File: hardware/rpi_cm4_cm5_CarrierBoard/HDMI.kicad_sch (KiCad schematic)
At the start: 12 parts, among them J4 2086581001, U18 AP22913W6-7

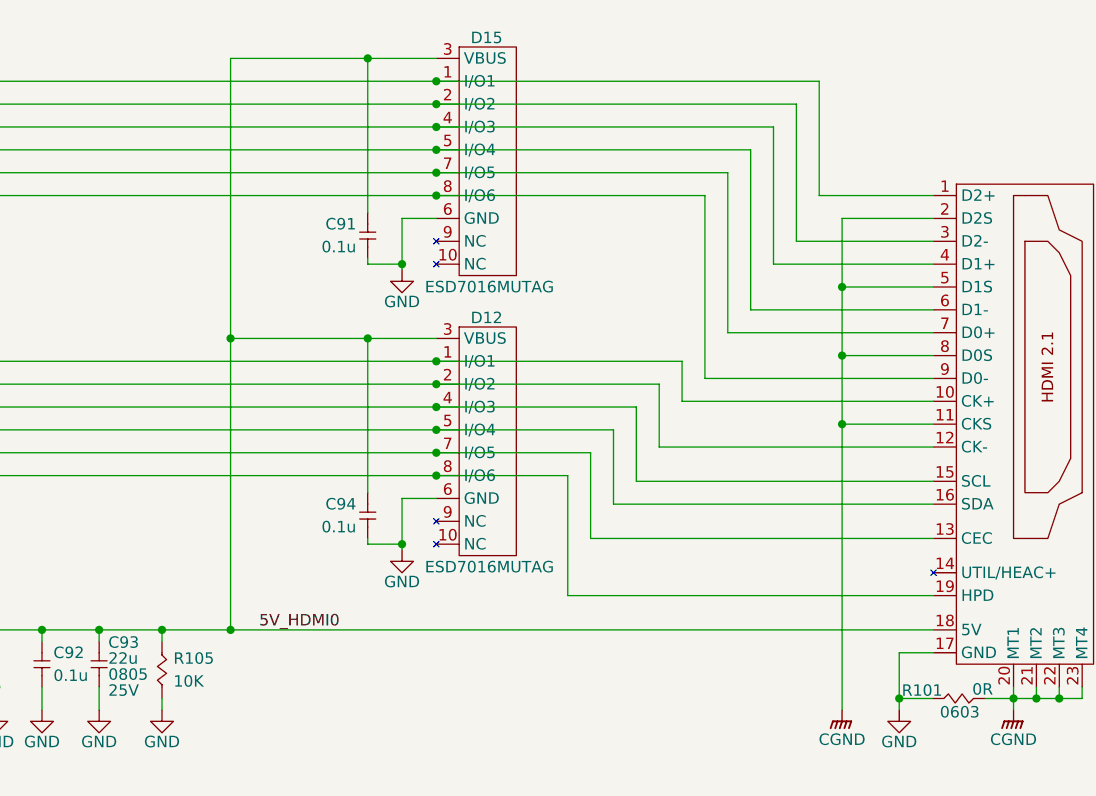
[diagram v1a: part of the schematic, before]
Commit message: Preliminary completion of RPI CMx schematics Cleaned up hierarchical root page
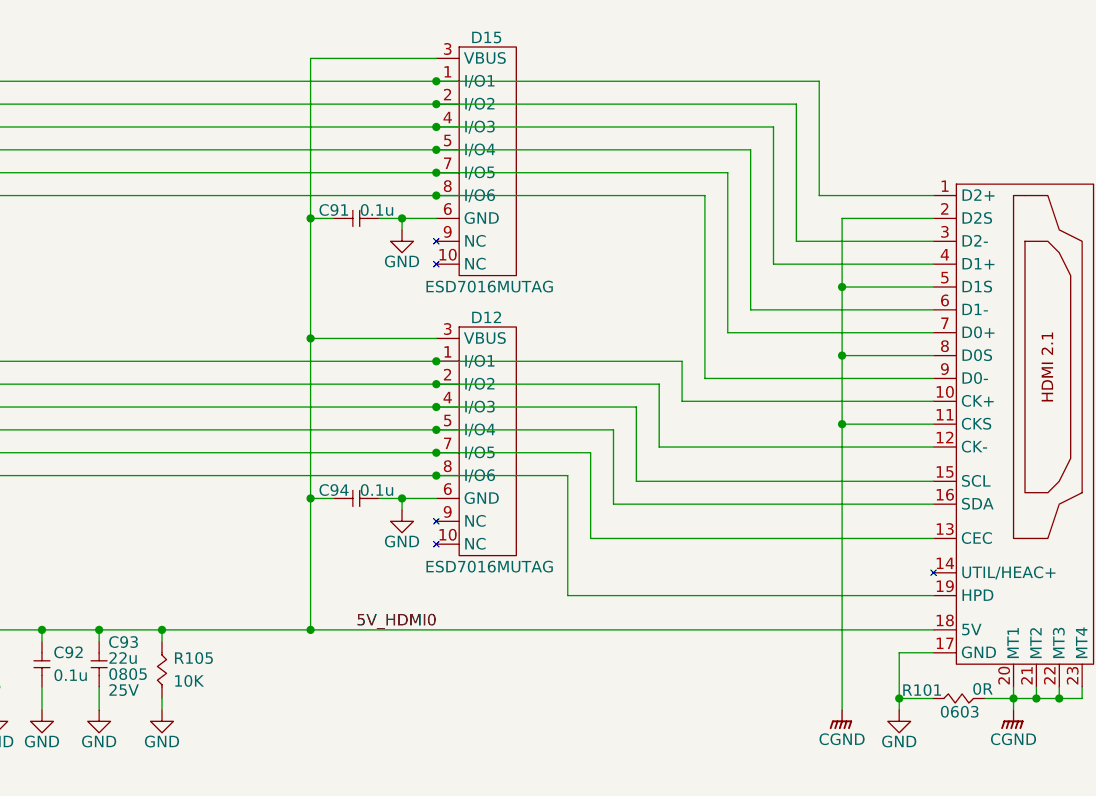
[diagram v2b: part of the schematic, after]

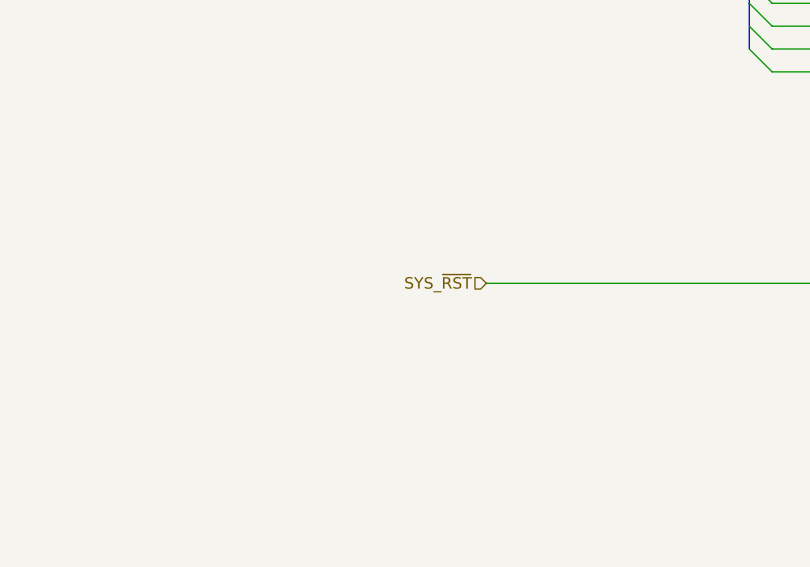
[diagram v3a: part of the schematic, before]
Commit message: Added power input protection & filter Added dedicated QWIIC connector on RPI CMx I2C6 bus Adjusted power table and PinMux Updated schematics accordingly
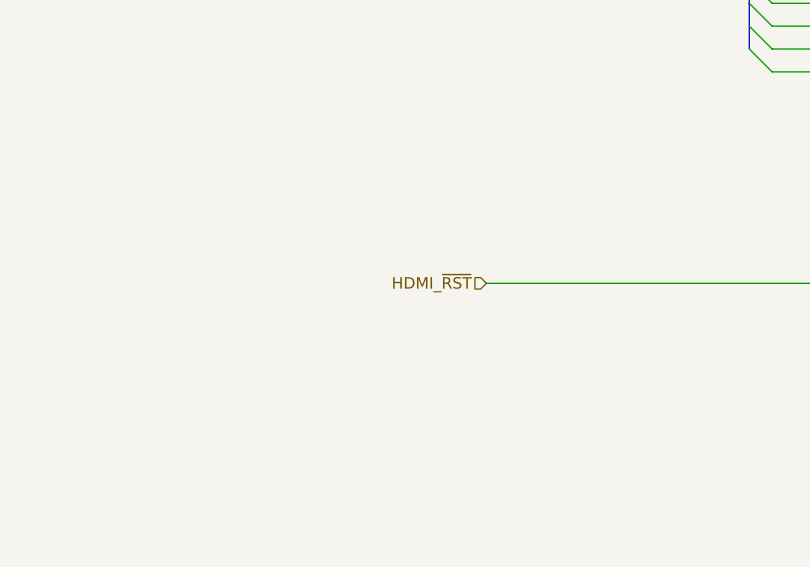
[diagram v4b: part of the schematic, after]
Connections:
- net SYS_~{RST} renamed HDMI_~{RST}
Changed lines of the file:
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@@
 		)
 	)
-	(hierarchical_label "SYS_~{RST}"
+	(hierarchical_label "HDMI_~{RST}"
 		(shape input)
 		(at 76.2 123.825 180)

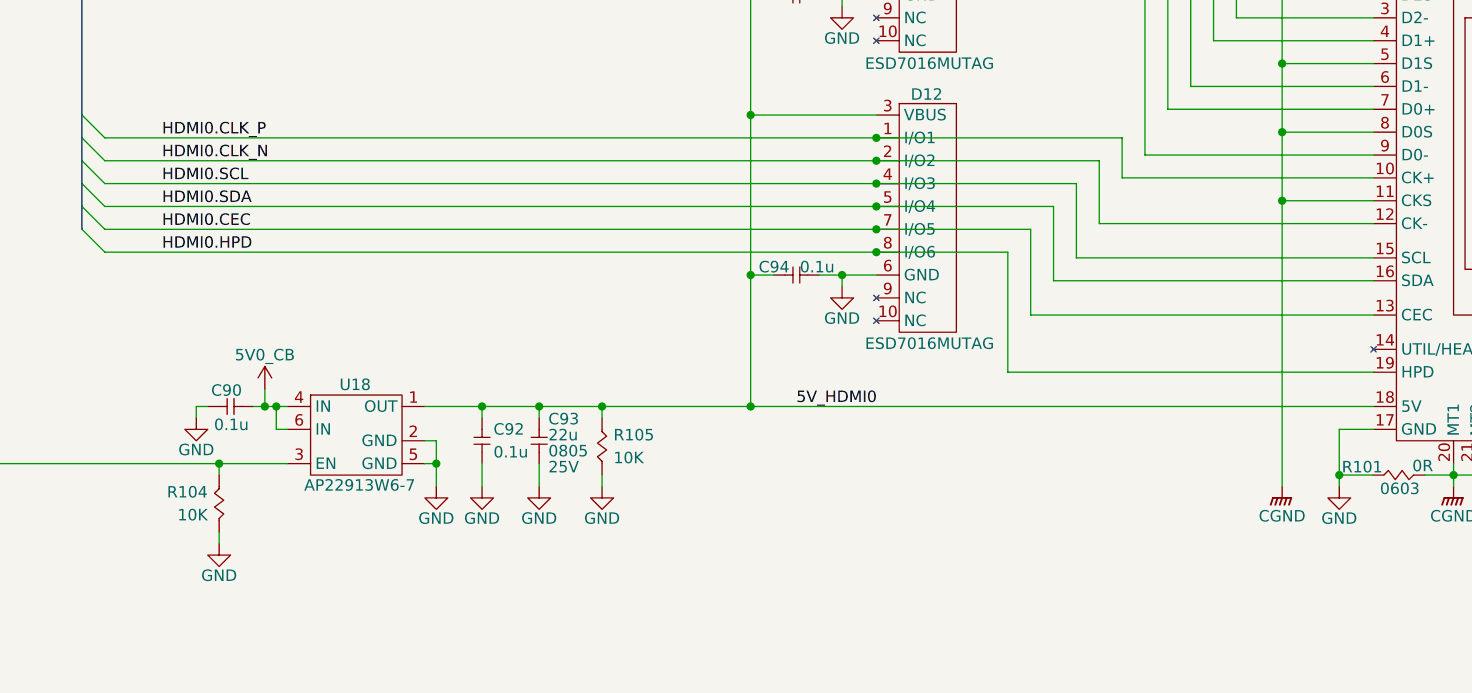
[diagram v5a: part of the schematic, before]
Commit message: Significant update in PCB layout; Completed preliminary high speed rules definition and fanout of differential pairs + GND vias. Started routing high speed signals Slight changes to Pinout based on component placement
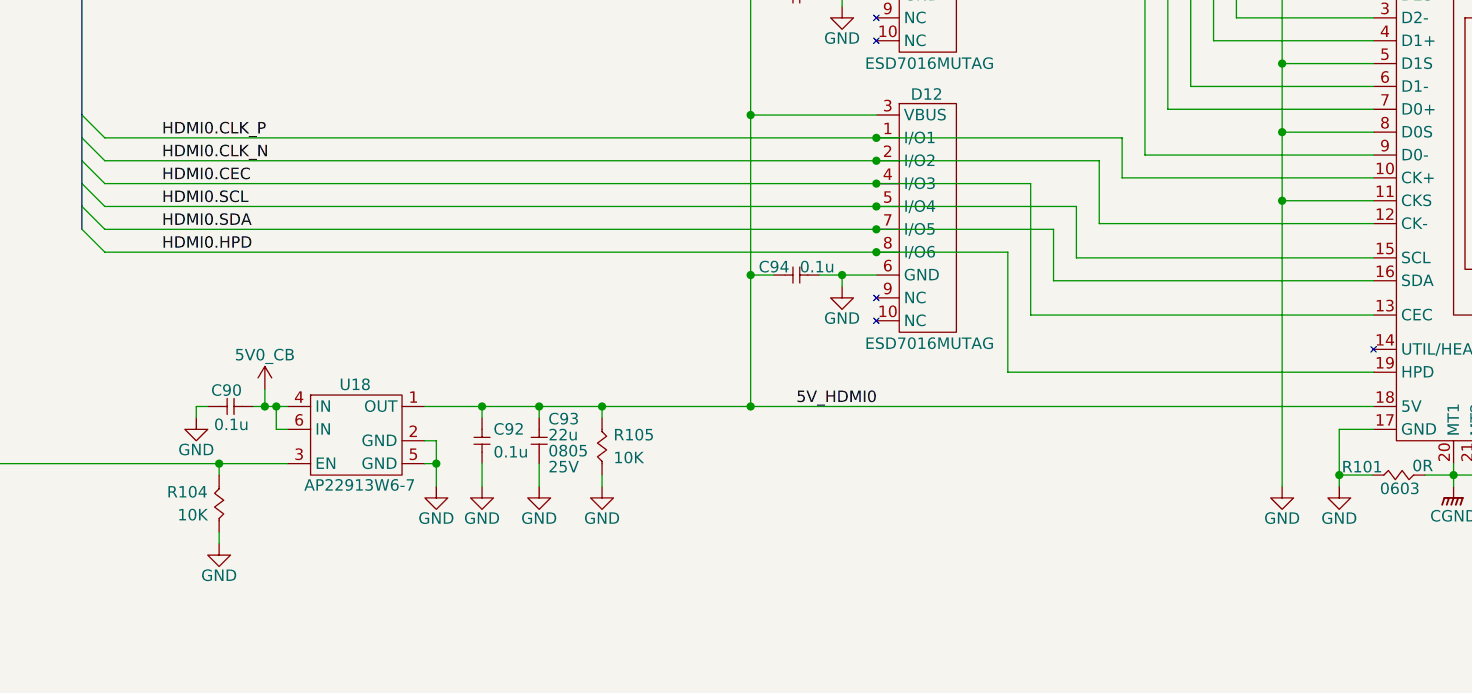
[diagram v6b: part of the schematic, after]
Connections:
- net CGND: no longer J4.11 (CKS), J4.2 (D2S), J4.5 (D1S), J4.8 (D0S)
- net GND: now also J4.11 (CKS), J4.2 (D2S), J4.5 (D1S), J4.8 (D0S)
- net HDMI0.CEC: now also D12.4 (I/O3); no longer D12.7 (I/O5)
- net HDMI0.SCL: now also D12.5 (I/O4); no longer D12.4 (I/O3)
- net HDMI0.SDA: now also D12.7 (I/O5); no longer D12.5 (I/O4)
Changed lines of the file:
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@@
+	)
+	(junction
+		(at 193.675 92.71)
+		(diameter 0)
+		(color 0 0 0 0)
 	)
 	(junction
@@
 	)
 	(junction
+		(at 193.675 95.25)
+		(diameter 0)
+		(color 0 0 0 0)
+	)
+	(junction
 		(at 193.675 56.515)
 		(diameter 0)
@@
 	)
 	(junction
-		(at 193.675 92.71)
+		(at 193.675 97.79)
 		(diameter 0)
 		(color 0 0 0 0)
@@
 	)
 	(junction
-		(at 193.675 95.25)
-		(diameter 0)
-		(color 0 0 0 0)
-	)
-	(junction
 		(at 193.675 66.675)
 		(diameter 0)
@@
 	)
 	(junction
-		(at 193.675 97.79)
-		(diameter 0)
-		(color 0 0 0 0)
-	)
-	(junction
 		(at 179.705 85.09)
 		(diameter 0)
@@
 	(wire
 		(pts
+			(xy 193.675 92.71) (xy 210.82 92.71)
+		)
+		(stroke
+			(width 0)
+			(type default)
+		)
+	)
+	(wire
+		(pts
 			(xy 238.76 86.995) (xy 238.76 94.615)
 		)
@@
 	(wire
 		(pts
-			(xy 213.36 103.505) (xy 213.36 95.25)
+			(xy 213.36 103.505) (xy 213.36 97.79)
 		)
 		(stroke
@@
 	(wire
 		(pts
+			(xy 193.675 97.79) (xy 213.36 97.79)
+		)
+		(stroke
+			(width 0)
+			(type default)
+		)
+	)
+	(wire
+		(pts
 			(xy 208.28 100.33) (xy 193.675 100.33)
 		)
@@
 	(wire
 		(pts
-			(xy 213.36 95.25) (xy 193.675 95.25)
-		)
-		(stroke
-			(width 0)
-			(type default)
-		)
-	)
-	(wire
-		(pts
 			(xy 124.46 117.475) (xy 125.73 117.475)
 		)
@@
 	(wire
 		(pts
-			(xy 210.82 97.79) (xy 193.675 97.79)
-		)
-		(stroke
-			(width 0)
-			(type default)
-		)
-	)
-	(wire
-		(pts
 			(xy 248.92 74.295) (xy 233.68 74.295)
 		)
@@
 	(wire
 		(pts
+			(xy 210.82 92.71) (xy 210.82 107.315)
+		)
+		(stroke
+			(width 0)
+			(type default)
+		)
+	)
+	(wire
+		(pts
 			(xy 220.98 87.63) (xy 193.675 87.63)
 		)
@@
 	(wire
 		(pts
-			(xy 215.9 100.965) (xy 215.9 92.71)
+			(xy 215.9 100.965) (xy 215.9 95.25)
 		)
 		(stroke
@@
 		)
 	)
-	(wire
-		(pts
-			(xy 215.9 92.71) (xy 193.675 92.71)
-		)
-		(stroke
-			(width 0)
-			(type default)
-		)
-	)
 	(bus
 		(pts
@@
 	(wire
 		(pts
-			(xy 210.82 107.315) (xy 210.82 97.79)
-		)
-		(stroke
-			(width 0)
-			(type default)
-		)
-	)
-	(wire
-		(pts
 			(xy 144.78 123.825) (xy 144.78 126.365)
 		)
@@
 		(pts
 			(xy 236.22 69.215) (xy 248.92 69.215)
+		)
+		(stroke
+			(width 0)
+			(type default)
+		)
+	)
+	(wire
+		(pts
+			(xy 193.675 95.25) (xy 215.9 95.25)
 		)
 		(stroke
@@
 		)
 	)
-	(label "HDMI0.CEC"
-		(at 114.3 97.79 0)
-		(effects
-			(font
-				(size 1.27 1.27)
-			)
-			(justify left bottom)
-		)
-	)
 	(label "HDMI0.HPD"
 		(at 114.3 100.33 0)
@@
 		)
 	)
-	(label "HDMI0.SCL"
+	(label "HDMI0.CEC"
 		(at 114.3 92.71 0)
+		(effects
+			(font
+				(size 1.27 1.27)
+			)
+			(justify left bottom)
+		)
+	)
+	(label "HDMI0.SDA"
+		(at 114.3 97.79 0)
 		(effects
 			(font
@@
 		)
 	)
-	(label "HDMI0.SDA"
-		(at 114.3 95.25 0)
-		(effects
-			(font
-				(size 1.27 1.27)
-			)
-			(justify left bottom)
-		)
-	)
 	(label "HDMI0.D0_P"
 		(at 114.3 66.675 0)
@@
 				(justify left)
 			)
+		)
+	)
+	(label "HDMI0.SCL"
+		(at 114.3 95.25 0)
+		(effects
+			(font
+				(size 1.27 1.27)
+			)
+			(justify left bottom)
 		)
 	)
@@
 				(path "/7dcdf741-90ca-4333-848c-806f4d64158e/da79d379-819b-4a23-bde6-cf0346f2b26a"
 					(reference "U18")
+					(unit 1)
+				)
+			)
+		)
+	)
+	(symbol
+		(lib_id "KiCad_Pwr_Symbols:GND")
+		(at 238.76 126.365 0)
+		(unit 1)
+		(exclude_from_sim no)
+		(in_bom yes)
+		(on_board yes)
+		(dnp no)
+		(property "Reference" "#PWR014"
+			(at 238.76 132.715 0)
+			(effects
+				(font
+					(size 1.27 1.27)
+				)
+				(hide yes)
+			)
+		)
+		(property "Value" "GND"
+			(at 238.76 129.921 0)
+			(effects
+				(font
+					(size 1.27 1.27)
+				)
+			)
+		)
+		(property "Footprint" ""
+			(at 238.76 126.365 0)
+			(effects
+				(font
+					(size 1.27 1.27)
+				)
+				(hide yes)
+			)
+		)
+		(property "Datasheet" ""
+			(at 238.76 126.365 0)
+			(effects
+				(font
+					(size 1.27 1.27)
+				)
+				(hide yes)
+			)
+		)
+		(property "Description" "Power symbol creates a global label with name \"GND\" , ground"
+			(at 238.76 126.365 0)
+			(effects
+				(font
+					(size 1.27 1.27)
+				)
+				(hide yes)
+			)
+		)
+		(pin "1"
+		)
+		(instances
+			(project "rpi_cm4_cm5_CarrierBoard"
+				(path "/7dcdf741-90ca-4333-848c-806f4d64158e/da79d379-819b-4a23-bde6-cf0346f2b26a"
+					(reference "#PWR014")
 					(unit 1)
 				)
@@
 					(unit 1)
 				)
-			)
-		)
-	)
-	(symbol
-		(lib_id "KiCad_Pwr_Symbols:GNDPWR")
-		(at 238.76 126.365 0)
-		(unit 1)
-		(exclude_from_sim no)
-		(in_bom yes)
-		(on_board yes)
-		(dnp no)
-		(property "Reference" "#PWR0150"
-			(at 238.76 131.445 0)
-			(effects
-				(font
-					(size 1.27 1.27)
-				)
-				(hide yes)
-			)
-		)
-		(property "Value" "CGND"
-			(at 238.76 129.667 0)
-			(effects
-				(font
-					(size 1.27 1.27)
-				)
-			)
-		)
-		(property "Footprint" ""
-			(at 238.76 127.635 0)
-			(effects
-				(font
-					(size 1.27 1.27)
-				)
-				(hide yes)
-			)
-		)
-		(property "Datasheet" ""
-			(at 238.76 127.635 0)
-			(effects
-				(font
-					(size 1.27 1.27)
-				)
-				(hide yes)
-			)
-		)
-		(property "Description" "Power symbol creates a global label with name \"GNDPWR\" , global ground"
-			(at 238.76 126.365 0)
-			(effects
-				(font
-					(size 1.27 1.27)
-				)
-				(hide yes)
-			)
-		)
-		(pin "1"
-		)
-		(instances
-			(project "rpi_cm4_cm5_CarrierBoard"
-				(path "/7dcdf741-90ca-4333-848c-806f4d64158e/da79d379-819b-4a23-bde6-cf0346f2b26a"
-					(reference "#PWR0150")
-					(unit 1)
-				)
